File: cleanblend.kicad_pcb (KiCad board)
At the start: 2 copper layers, 30 x 30 mm, 36 parts, among them U1 TL074

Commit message: TMP breadboard design
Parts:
- removed the H1 at (83.9, 77.8)
- removed the H2 at (83.9, 80.3)
- added H1: GND, pedal-component-footprint:PinHeader_1x01_P2.54mm_Long_Front_Back, F.Cu at (83.8, 121.3)
- added H1: GND, pedal-component-footprint:PinHeader_1x01_P2.54mm_Long_Front_Back, F.Cu at (83.9, 78.7)
- added H2: +9V, pedal-component-footprint:PinHeader_1x01_P2.54mm_Long_Front_Back, F.Cu at (83.9, 123.8)
- added H2: +9V, pedal-component-footprint:PinHeader_1x01_P2.54mm_Long_Front_Back, F.Cu at (83.9, 76.2)
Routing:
- net MixIn2: track 56.1 -> 0.00 mm, vias 3 -> 0
- net Vref: track 53.3 -> 0.00 mm, vias 6 -> 0
- net MixIn1: track 50.0 -> 0.00 mm, vias 2 -> 0
- net Net-(C8-Pad1): track 32.4 -> 0.00 mm
- net Net-(C5-Pad2): track 26.9 -> 0.00 mm, vias 2 -> 0
- net Net-(C6-Pad2): track 24.0 -> 0.00 mm, vias 2 -> 0
- net Net-(C4-Pad2): track 21.1 -> 0.00 mm, vias 2 -> 0
- net +9V: track 18.9 -> 0.00 mm, vias 4 -> 0
- net MixOut: track 18.3 -> 0.00 mm, vias 1 -> 0
- net Net-(C3-Pad1): track 17.6 -> 0.00 mm
- net CleanCopy2: track 16.7 -> 0.00 mm, vias 2 -> 0
- net Net-(R4-Pad1): track 11.4 -> 0.00 mm, vias 1 -> 0
- net Net-(C4-Pad1): track 10.5 -> 0.00 mm
- net CleanCopy1: track 10.1 -> 0.00 mm, vias 2 -> 0
- net GND: track 9.60 -> 0.00 mm, vias 8 -> 0
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- removed copper zone on F.Cu, net +9V
- removed copper zone on B.Cu, net GND
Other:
- board size 30 x 30 mm -> 30 x 50.7 mm

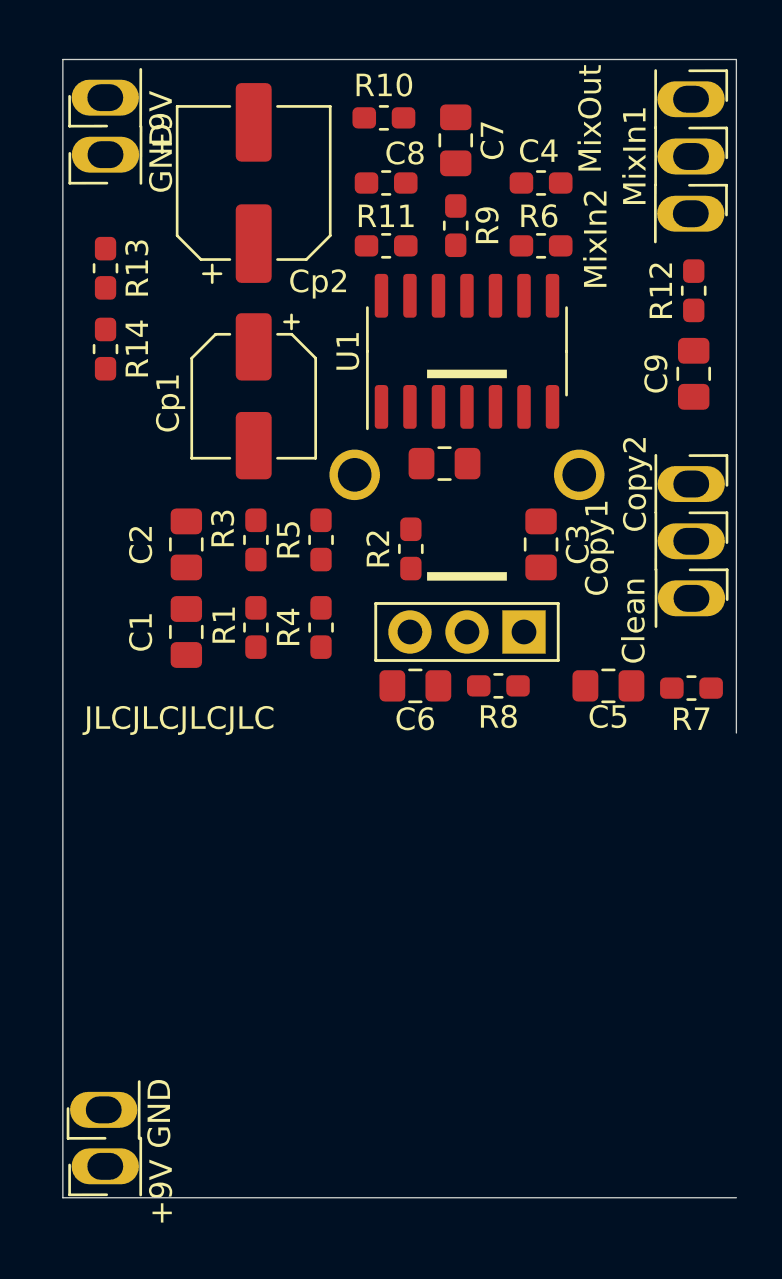
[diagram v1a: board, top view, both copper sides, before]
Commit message: SplitNMix breadboard start
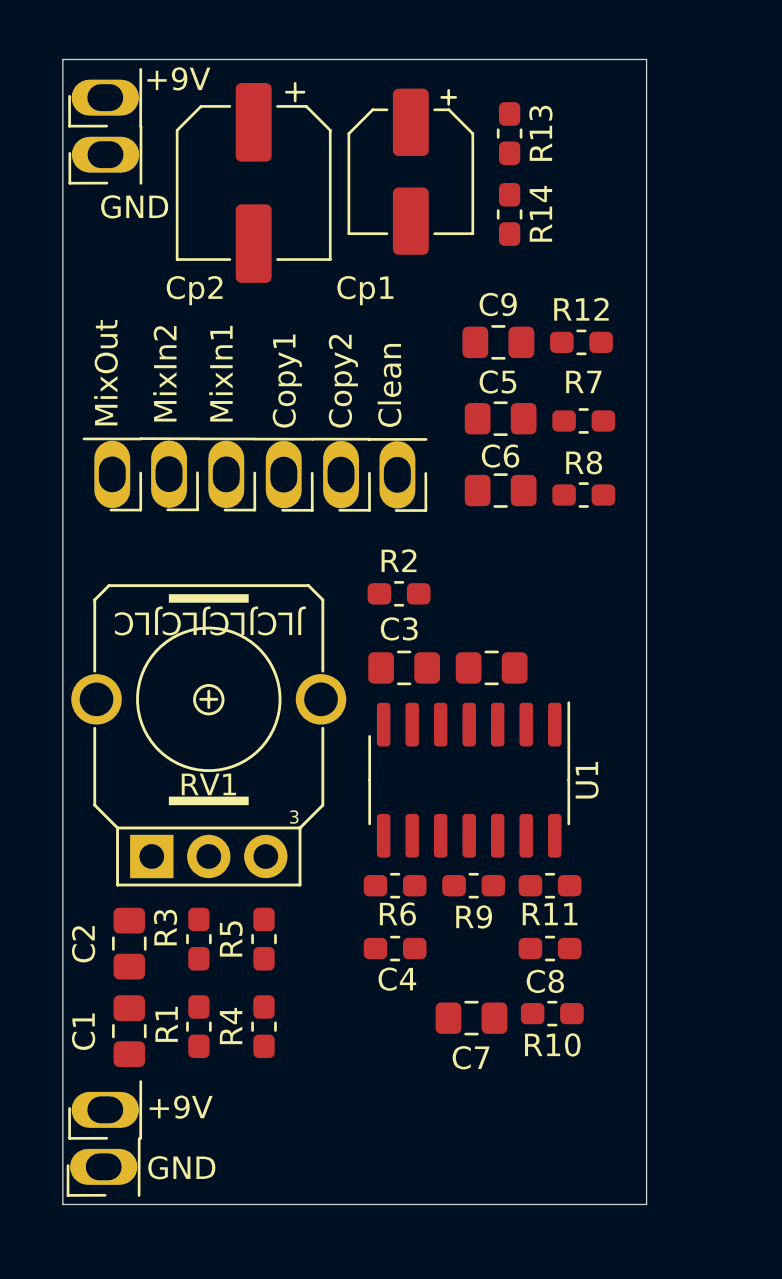
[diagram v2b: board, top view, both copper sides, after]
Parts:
- RV1: moved to B.Cu
- moved R10 40.6 mm to (103.8, 117.0), turned to 180 degrees
- moved C7 39.1 mm to (100.2, 117.2), turned to 180 degrees
- moved C8 34.9 mm to (103.7, 114.1), turned to 180 degrees
- moved C4 34.7 mm to (96.8, 114.1), turned to 0 degrees
- moved H8 30.7 mm to (84.2, 93.0), turned to 180 degrees
- moved R11 29.4 mm to (103.7, 111.3), turned to 0 degrees
- moved R9 29.4 mm to (100.3, 111.3), turned to 180 degrees
- moved R6 29.2 mm to (96.8, 111.3), turned to 180 degrees
- moved H7 26.0 mm to (86.7, 93.0), turned to 180 degrees
- moved H6 25.1 mm to (89.3, 93.0), turned to 180 degrees
- moved U1 19.1 mm to (100.1, 106.6), turned to 270 degrees
- moved R13 19.0 mm to (101.9, 77.8)
- moved R14 19.0 mm to (101.9, 81.4)
- moved H4 18.4 mm to (91.8, 93.0), turned to 180 degrees
- moved C1 18.0 mm to (85.0, 117.8)
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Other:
- board size 30 x 50.7 mm -> 26 x 51 mm

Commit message: Breadboard version
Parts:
- turned R8 to 0 degrees
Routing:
- net +9V: track 0.00 -> 100.6 mm, vias 0 -> 5
- net Vref: track 0.00 -> 71.5 mm, vias 0 -> 5
- net Net-(C8-Pad1): track 0.00 -> 40.5 mm
- net MixIn2: track 0.00 -> 35.9 mm
- net MixIn1: track 0.00 -> 33.5 mm, vias 0 -> 2
- net MixOut: track 0.00 -> 25.1 mm
- net Net-(R4-Pad1): track 0.00 -> 19.3 mm
- net Net-(C6-Pad2): track 0.00 -> 18.0 mm
- net Net-(C4-Pad2): track 0.00 -> 16.2 mm, vias 0 -> 2
- net CleanCopy1: track 0.00 -> 16.2 mm
- net CleanCopy2: track 0.00 -> 15.7 mm
- net Net-(C5-Pad2): track 0.00 -> 15.5 mm, vias 0 -> 2
- net GND: track 0.00 -> 12.1 mm, vias 0 -> 7
- net Net-(C3-Pad1): track 0.00 -> 11.4 mm
- net Net-(C1-Pad1): track 0.00 -> 11.4 mm
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- added copper zone on B.Cu, net GND
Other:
- net class Power: trace_width 0.45 -> 0.5
